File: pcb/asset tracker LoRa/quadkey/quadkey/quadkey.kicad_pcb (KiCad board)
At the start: 2 copper layers, 42.1 x 72.6 mm, 33 parts, among them CON1 jtag, J1 USB_B_Mini, U1 MCP73831, U2 TPS63001, U3 nRF52810-QFxx, Y1 326MhZ

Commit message: code
code
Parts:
- removed J1: USB_B_Mini, connectors_user:AMPHENOL_10118192-0001LF
- added con1: USB_micro, connectors_user:MILLMAX_897-43-005-00-100001, F.Cu at (98.0, 114.7)
- C9: moved to F.Cu
- Y1: value 326MhZ -> 32MhZ
- moved C9 1.74 mm to (96.1, 58.6)
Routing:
- net GND: track 78.9 -> 87.8 mm, vias 19 -> 18
- net Net-(L1-Pad1): track 7.70 -> 5.22 mm
- net Net-(C9-Pad2): track 4.40 -> 5.87 mm, vias 1 -> 0
- net /mcu/SWDIO: track 14.4 -> 13.5 mm

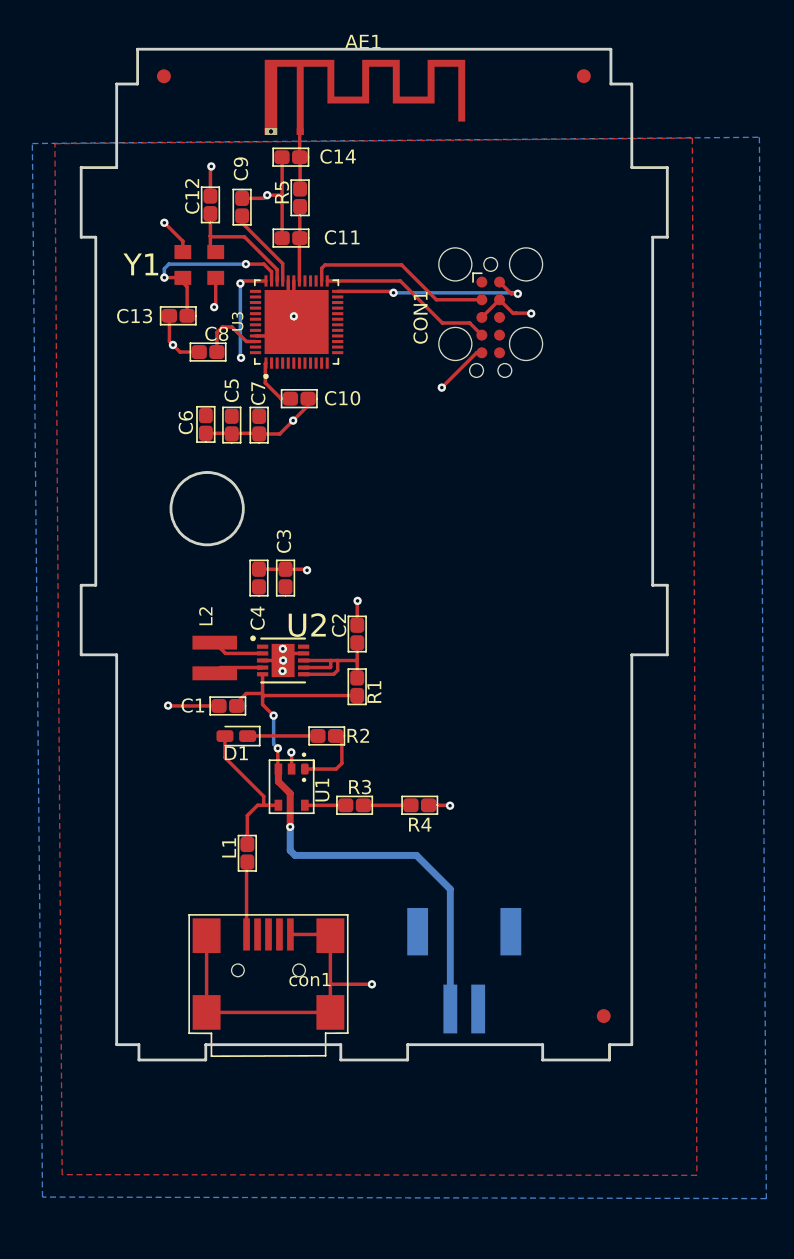
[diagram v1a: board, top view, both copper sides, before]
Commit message: versie2
aan versie 2 begonnen met tekenen en code beginnen schrijven voor quadkey
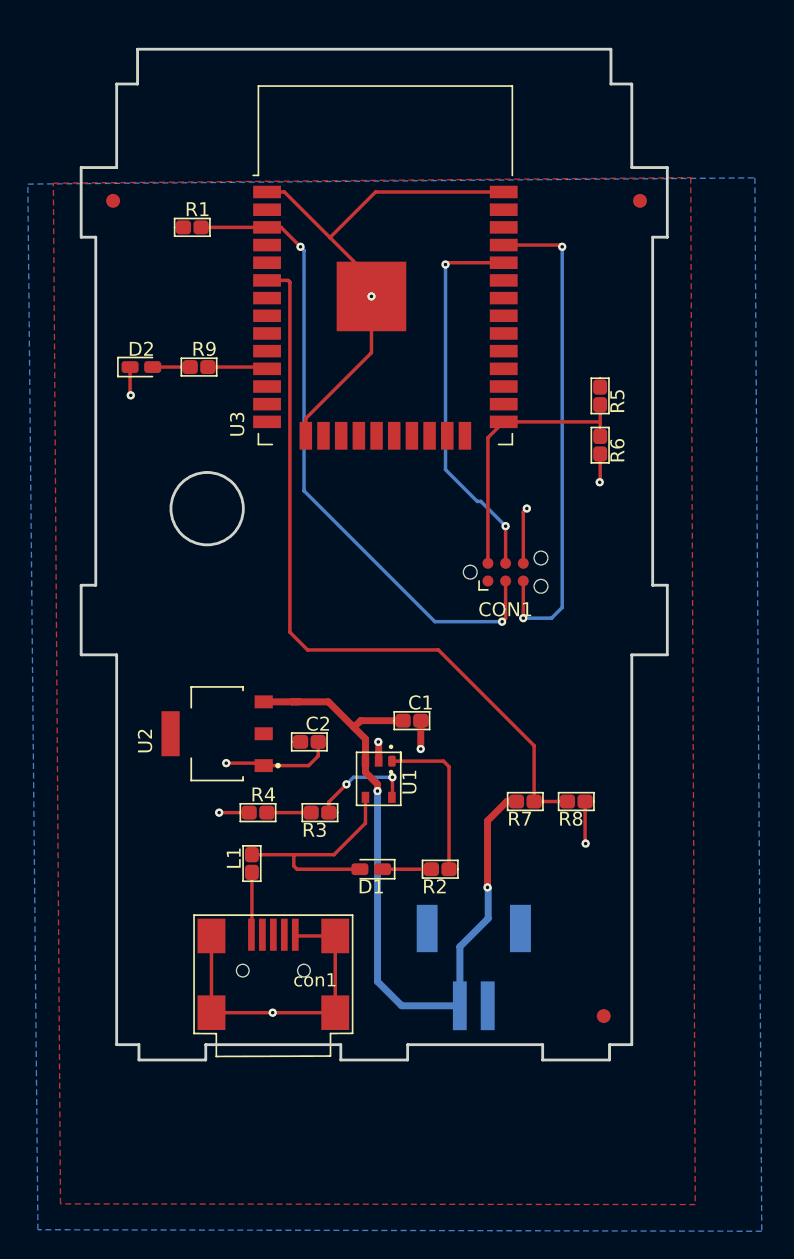
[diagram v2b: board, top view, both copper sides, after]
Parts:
- removed AE1: Antenna, vanalles:Texas_SWRA117D_2.4GHz_Right
- removed C10, C6, C7: 100nF, vanalles:0603
- removed C11, C14: NM, vanalles:0603
- removed C12, C13: 12pF, vanalles:0603
- removed C3, C4: 10uF, vanalles:0603
- removed C5: 4.7uF, vanalles:0603
- removed C8: 1uF, vanalles:0603
- removed C9: 100pF, vanalles:0603
- removed L2: 2.2uH, vanalles:WURTH_744025001
- removed Y1: 32MhZ, vanalles:OSCCC320X250X90L80X100N
- added D2: LED, halfgeleiders:led0603, F.Cu at (88.9, 70.1)
- added R6: NM, vanalles:0603RL, F.Cu at (121.9, 75.7)
- added R7: 100K, vanalles:0603RL, F.Cu at (116.5, 101.3)
- added R8: 100k, vanalles:0603RL, F.Cu at (120.1, 101.3)
- added R9: nm, vanalles:0603RL, F.Cu at (93.0, 70.1)
- C2: value 0.1uF -> 10uF
- CON1: value jtag -> TAGconnect_ESP; footprint connectors_user:Tag-Connect_TC2050-IDC-FP_2x05_P1.27mm_Vertical -> connectors_user:Tag-Connect_TC2030-IDC-NL_2x03_P1.27mm_Vertical
- R1: value 100 -> 10K
- R5: value 0 -> 10K
- U2: value TPS63001 -> AMS1117-3.3; footprint halfgeleiders:SON50P300X300X100-11N -> halfgeleiders:SOT229P700X180-4N
- U3: value nRF52810-QFxx -> ESP32-WROOM; footprint halfgeleiders:nrf -> Module:ESP32-WROOM-32
- moved R1 35.1 mm to (92.6, 60.1), turned to 0 degrees
- moved R5 25.8 mm to (121.8, 72.2), turned to -90 degrees
- moved CON1 18.3 mm to (115.1, 84.8), turned to 0 degrees
- moved D1 13.6 mm to (105.4, 106.2)
- moved C1 13.3 mm to (108.3, 95.5), turned to 0 degrees
- moved R2 12.6 mm to (110.4, 106.2)
- moved R4 11.6 mm to (97.3, 102.1), turned to 0 degrees
- moved REF** 9.82 mm to (124.7, 58.2)
- moved REF** 9.66 mm to (86.9, 58.2)
- moved C2 8.47 mm to (101.0, 97.0), turned to 0 degrees
- moved U2 7.08 mm to (94.3, 96.4), turned to 90 degrees
- moved U3 6.47 mm to (106.4, 65.8), turned to 0 degrees
- moved U1 6.28 mm to (106.0, 99.7)
- moved R3 2.55 mm to (101.7, 102.1), turned to 180 degrees
- moved L1 0.81 mm to (96.8, 105.8)
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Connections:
- C2 pad 1: Net-(C2-Pad1) -> +3V3
- CON1 pad 2: /mcu/SWDIO -> /mcu/GPIO0
- CON1 pad 3: GND -> /mcu/RESET
- CON1 pad 4: /mcu/SWDCLK -> /mcu/RX
- CON1 pad 5: GND -> /mcu/TX
- CON1 pad 6: unconnected-(CON1-Pad6) -> GND
- R1 pad 1: Net-(C2-Pad1) -> +3V3
- R1 pad 2: VBAT -> /mcu/RESET
- R5 pad 1: Net-(C11-Pad1) -> +3V3
- R5 pad 2: Net-(AE1-Pad1) -> /mcu/GPIO0
- U2 pad 1: +3V3 -> GND
- U2 pad 2: Net-(L2-Pad2) -> +3V3
- U2 pad 3: GND -> VBAT
- U2 pad 4: Net-(L2-Pad1) -> unconnected-(U2-Pad4)
- U3 pad 1: Net-(C10-Pad2) -> GND
- U3 pad 11: unconnected-(U3-Pad11) -> Net-(U3-Pad11)
- U3 pad 13: +3V3 -> unconnected-(U3-Pad13)
- U3 pad 15: unconnected-(U3-Pad15) -> GND
- U3 pad 2: unconnected-(U3-Pad2) -> +3V3
- U3 pad 24: /mcu/RST -> unconnected-(U3-Pad24)
- U3 pad 25: /mcu/SWDCLK -> /mcu/GPIO0
- U3 pad 26: /mcu/SWDIO -> unconnected-(U3-Pad26)
- U3 pad 3: unconnected-(U3-Pad3) -> /mcu/RESET
- U3 pad 30: Net-(C11-Pad1) -> unconnected-(U3-Pad30)
- U3 pad 31: GND -> unconnected-(U3-Pad31)
- U3 pad 32: GND -> unconnected-(U3-Pad32)
- U3 pad 33: Net-(C9-Pad2) -> unconnected-(U3-Pad33)
- U3 pad 34: Net-(C12-Pad1) -> /mcu/RX
- U3 pad 35: Net-(C13-Pad1) -> /mcu/TX
- U3 pad 36: +3V3 -> unconnected-(U3-Pad36)
- U3 pad 38: unconnected-(U3-Pad38) -> GND
- U3 pad 39: unconnected-(U3-Pad39) -> GND
- U3 pad 6: unconnected-(U3-Pad6) -> /mcu/VM
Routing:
- net /mcu/VM: track 0.00 -> 54.2 mm
- net /mcu/RESET: track 0.00 -> 46.5 mm, vias 0 -> 2
- net /mcu/TX: track 0.00 -> 35.9 mm, vias 0 -> 2
- net /mcu/RX: track 0.00 -> 27.6 mm, vias 0 -> 2
- net /mcu/GPIO0: track 0.00 -> 19.8 mm
- net /mcu/RST: track 14.7 -> 0.00 mm, vias 2 -> 0
- net /mcu/SWDIO: track 13.5 -> 0.00 mm
- net Net-(C13-Pad1): track 13.4 -> 0.00 mm, vias 2 -> 0
- net /mcu/SWDCLK: track 12.7 -> 0.00 mm
- net Net-(C2-Pad1): track 12.1 -> 0.00 mm
- net VBAT: track 44.1 -> 53.9 mm, vias 3 -> 2
- net Net-(C12-Pad1): track 9.52 -> 0.00 mm
- net +3V3: track 7.28 -> 0.00 mm, vias 2 -> 0
- net Net-(R2-Pad1): track 4.98 -> 11.6 mm
- net VBUS: track 10.7 -> 16.6 mm
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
